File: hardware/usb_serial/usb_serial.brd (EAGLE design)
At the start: 30.5 x 19 mm, 16 parts, among them J1 MICRO-USB

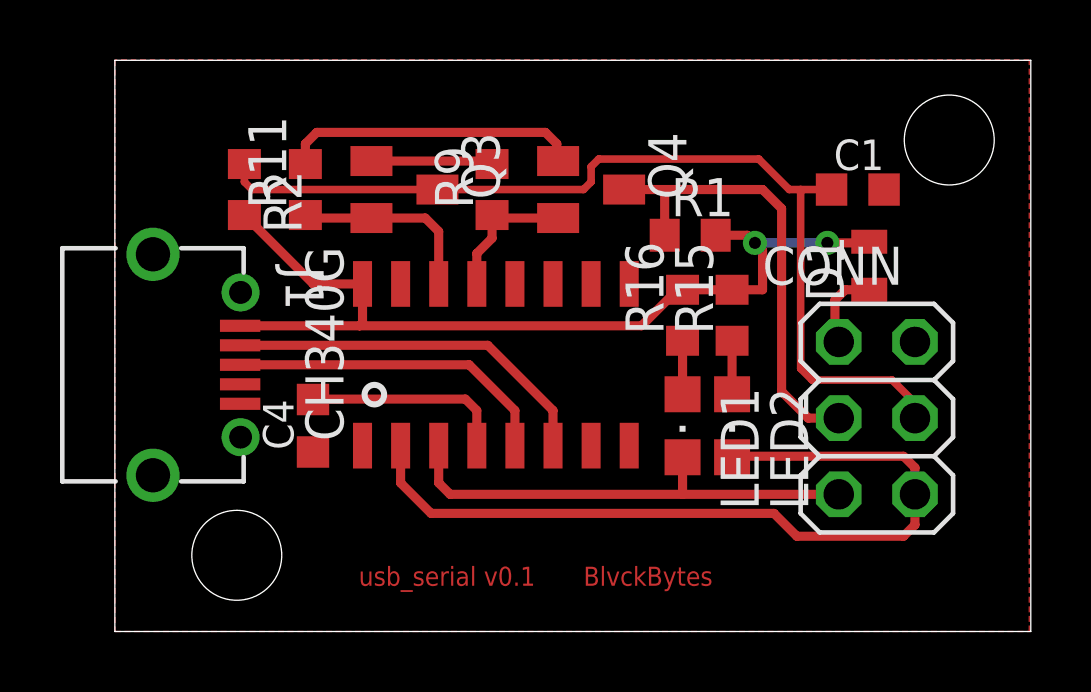
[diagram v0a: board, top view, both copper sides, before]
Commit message: Migrated back to ESP32, updated pins in code and updated hardware, also updated readme
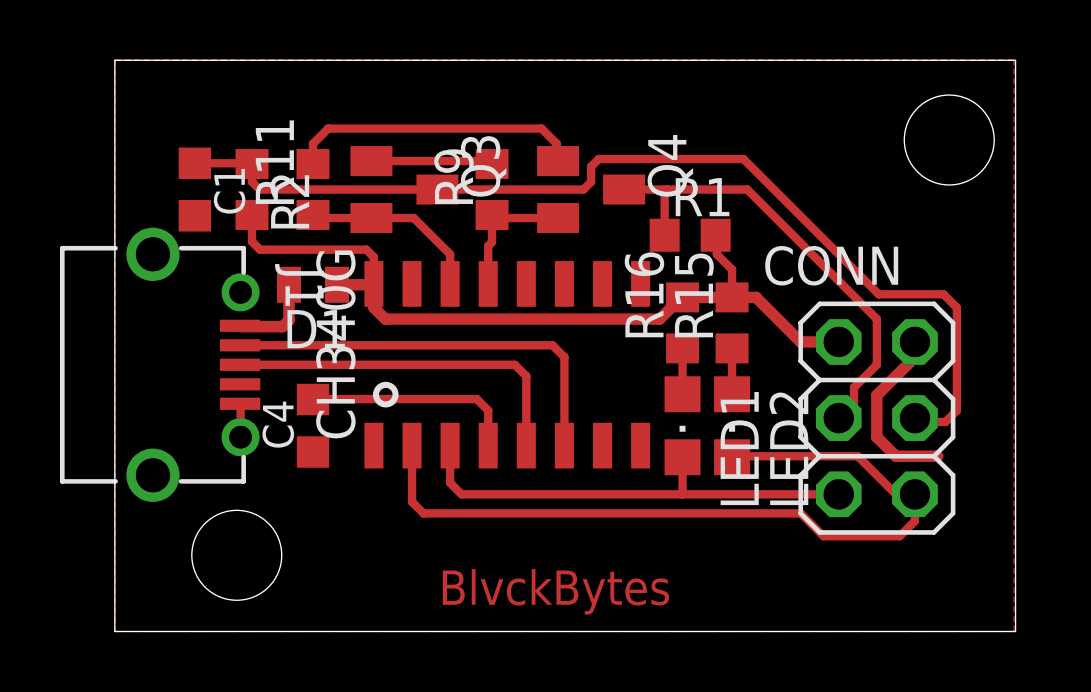
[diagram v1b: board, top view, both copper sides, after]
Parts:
- moved C1 22.1 mm to (3.94, 75.7), turned to 270 degrees
- moved D1 18.6 mm to (7.87, 72.5), turned to 180 degrees
- moved U$3 0.38 mm to (14.4, 69.8)
- moved R15 0.25 mm to (21.8, 71.2)
- moved R16 0.25 mm to (20.2, 71.2)
- moved R11 0.25 mm to (7.87, 75.7)
- moved R2 0.25 mm to (5.84, 75.7)
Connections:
- net +5V: now also CONN.1, D1.C; no longer D1.A, J1.VCC
- net N$1: now also D1.A, J1.VCC; no longer CONN.1, D1.C
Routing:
- net GND: track 0.00 -> 6.61 mm
- net +5V: track 31.2 -> 27.0 mm, vias 2 -> 0
- net RESET: track 32.2 -> 34.1 mm
- net N$9: track 12.5 -> 13.9 mm
- net N$8: track 11.0 -> 12.0 mm
- net RX: track 27.5 -> 26.9 mm
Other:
- board size 30.5 x 19 mm -> 30 x 19 mm
- board text removed: "usb_serial v0.1"
